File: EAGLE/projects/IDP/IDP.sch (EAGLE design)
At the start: 2 parts, among them M1 IDP_PROTOBOARD

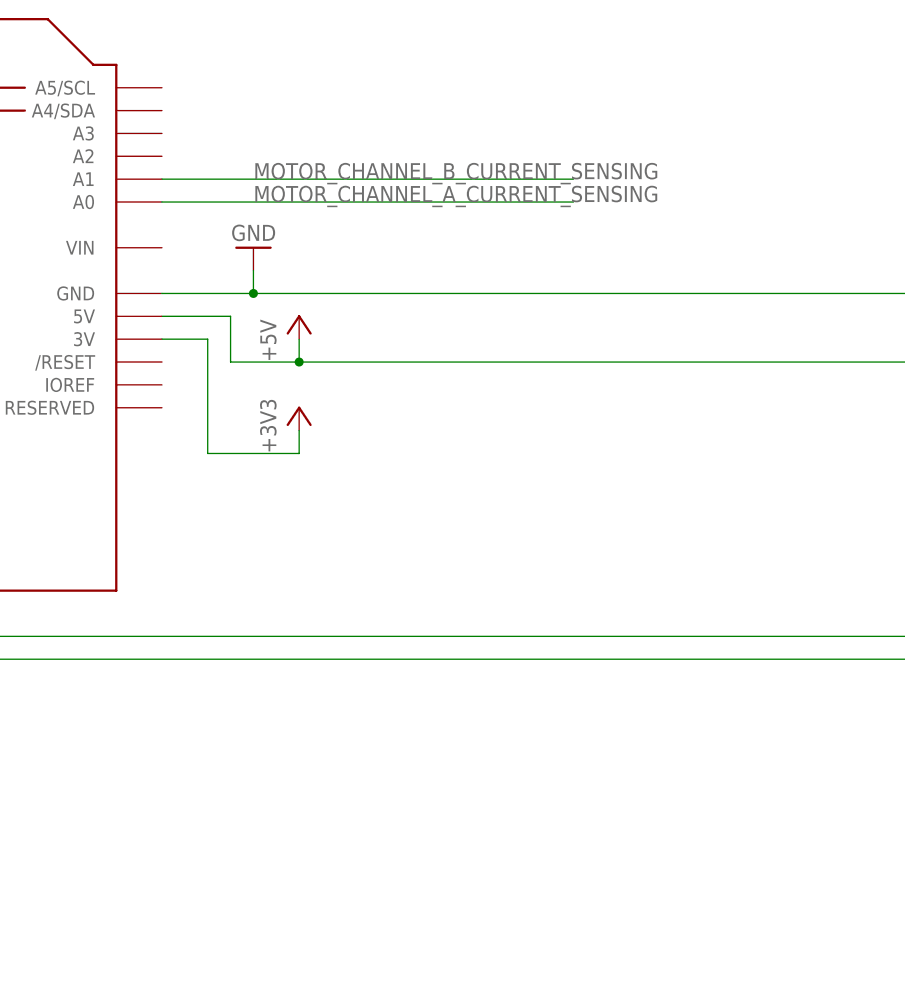
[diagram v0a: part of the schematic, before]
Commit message: Added IR sensor
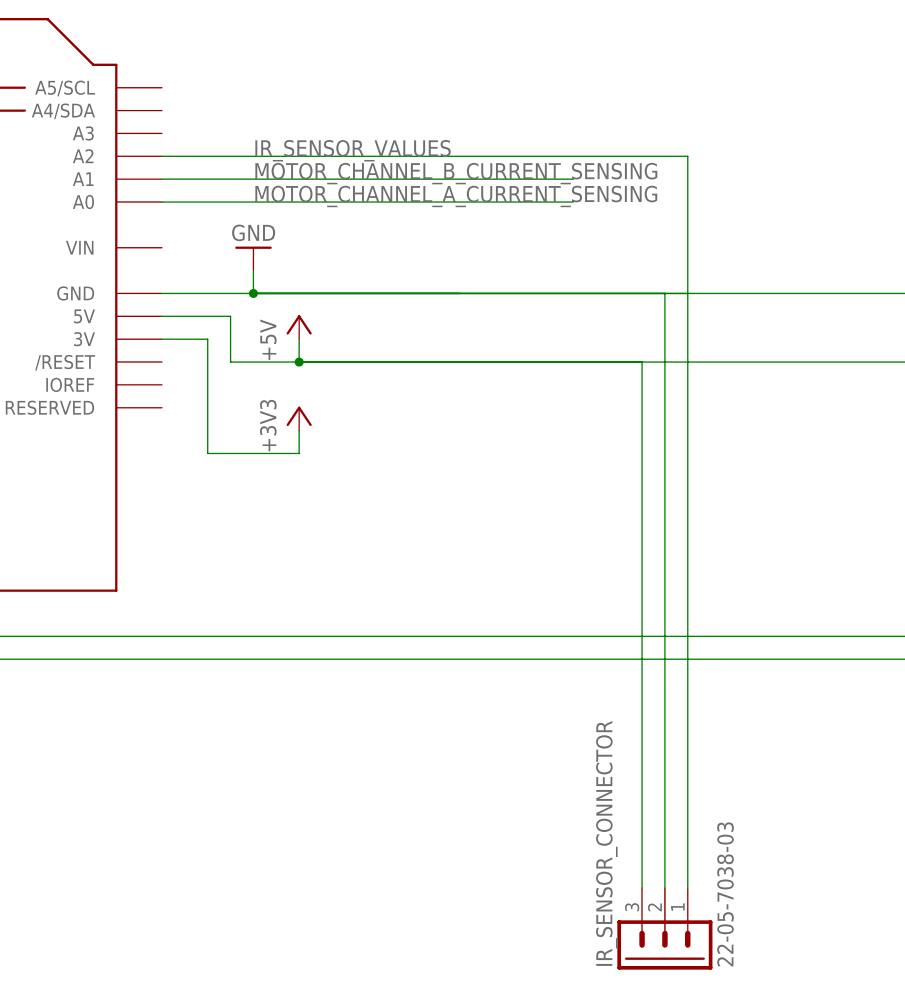
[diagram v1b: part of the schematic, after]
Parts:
- added IR_SENSOR_CONNECTOR: 22-05-7038-03, IDP_library:22-05-7038-03
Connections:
- new net IR_SENSOR_VALUES: IR_SENSOR_CONNECTOR.1, M1.A2
- net +5V: now also IR_SENSOR_CONNECTOR.3
- net GND: now also IR_SENSOR_CONNECTOR.2
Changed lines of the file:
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@@
 <part name="GND1" library="IDP_library" deviceset="GND" device=""/>
 <part name="U$1" library="diy-modules" deviceset="ULTRASONIC-HC-SR04" device=""/>
+<part name="IR_SENSOR_CONNECTOR" library="IDP_library" deviceset="22-?-03" device="05-7038" package3d_urn="urn:adsk.eagle:package:8078646/1"/>
 </parts>
 <sheets>
@@
 <attribute name="VALUE" x="251.46" y="119.38" size="1.778" layer="95"/>
 </instance>
+<instance part="IR_SENSOR_CONNECTOR" gate="G$1" x="218.44" y="22.86" smashed="yes" rot="R90">
+<attribute name="VALUE" x="226.06" y="21.59" size="1.778" layer="96" rot="R90"/>
+<attribute name="NAME" x="212.598" y="21.59" size="1.778" layer="95" rot="R90"/>
+</instance>
 </instances>
 <busses>
@@
 <pinref part="U$1" gate="G$1" pin="GND"/>
 <wire x1="279.4" y1="88.9" x2="279.4" y2="91.44" width="0.1524" layer="91"/>
+<wire x1="172.72" y1="96.52" x2="195.58" y2="96.52" width="0.1524" layer="91"/>
+<pinref part="IR_SENSOR_CONNECTOR" gate="G$1" pin="2"/>
+<wire x1="172.72" y1="96.52" x2="218.44" y2="96.52" width="0.1524" layer="91"/>
+<wire x1="218.44" y1="96.52" x2="218.44" y2="30.48" width="0.1524" layer="91"/>
+<wire x1="172.72" y1="96.52" x2="220.98" y2="96.52" width="0.1524" layer="91"/>
 </segment>
 </net>
@@
 <wire x1="177.8" y1="88.9" x2="271.78" y2="88.9" width="0.1524" layer="91"/>
 <junction x="177.8" y="88.9"/>
+<wire x1="177.8" y1="88.9" x2="187.96" y2="88.9" width="0.1524" layer="91"/>
+<wire x1="177.8" y1="88.9" x2="213.36" y2="88.9" width="0.1524" layer="91"/>
+<pinref part="IR_SENSOR_CONNECTOR" gate="G$1" pin="3"/>
+<wire x1="177.8" y1="88.9" x2="215.9" y2="88.9" width="0.1524" layer="91"/>
+<wire x1="215.9" y1="88.9" x2="215.9" y2="30.48" width="0.1524" layer="91"/>
 </segment>
 </net>
@@
 </segment>
 </net>
+<net name="IR_SENSOR_VALUES" class="0">
+<segment>
+<pinref part="M1" gate="G$1" pin="A2"/>
+<wire x1="162.56" y1="111.76" x2="220.98" y2="111.76" width="0.1524" layer="91"/>
+<pinref part="IR_SENSOR_CONNECTOR" gate="G$1" pin="1"/>
+<wire x1="220.98" y1="111.76" x2="220.98" y2="30.48" width="0.1524" layer="91"/>
+<label x="172.72" y="111.76" size="1.778" layer="95"/>
+</segment>
+</net>
 </nets>
 </sheet>
@@
 </schematic>
 </drawing>
+<compatibility>
+<note version="8.3" severity="warning">
+Since Version 8.3, EAGLE supports URNs for individual library
+assets (packages, symbols, and devices). The URNs of those assets
+will not be understood (or retained) with this version.
+</note>
+<note version="8.3" severity="warning">
+Since Version 8.3, EAGLE supports the association of 3D packages
+with devices in libraries, schematics, and board files. Those 3D
+packages will not be understood (or retained) with this version.
+</note>
+</compatibility>
 </eagle>
